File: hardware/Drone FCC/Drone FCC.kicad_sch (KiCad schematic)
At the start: 3 parts, among them J21 Micro_SD_Card_Det_Hirose_DM3AT, J23 47589-0001, U3 STM32F746ZGTx

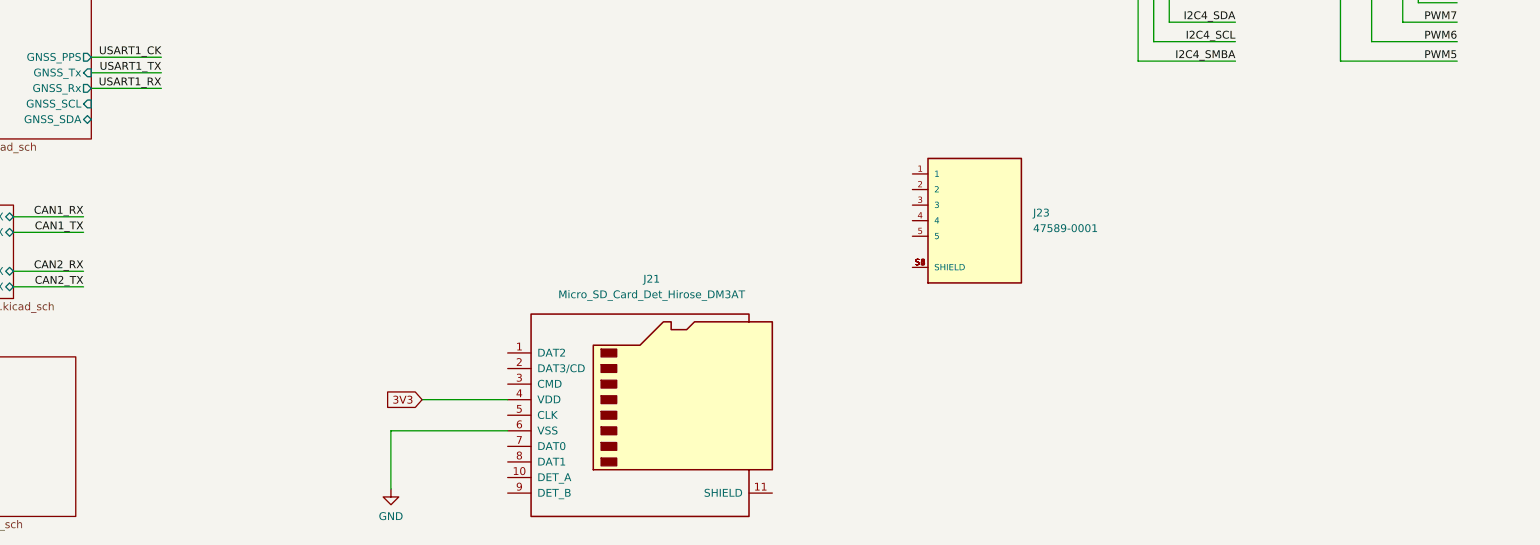
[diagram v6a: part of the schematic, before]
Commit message: DSM: deleted dupont conn, PPM: deleted DF-13 conn
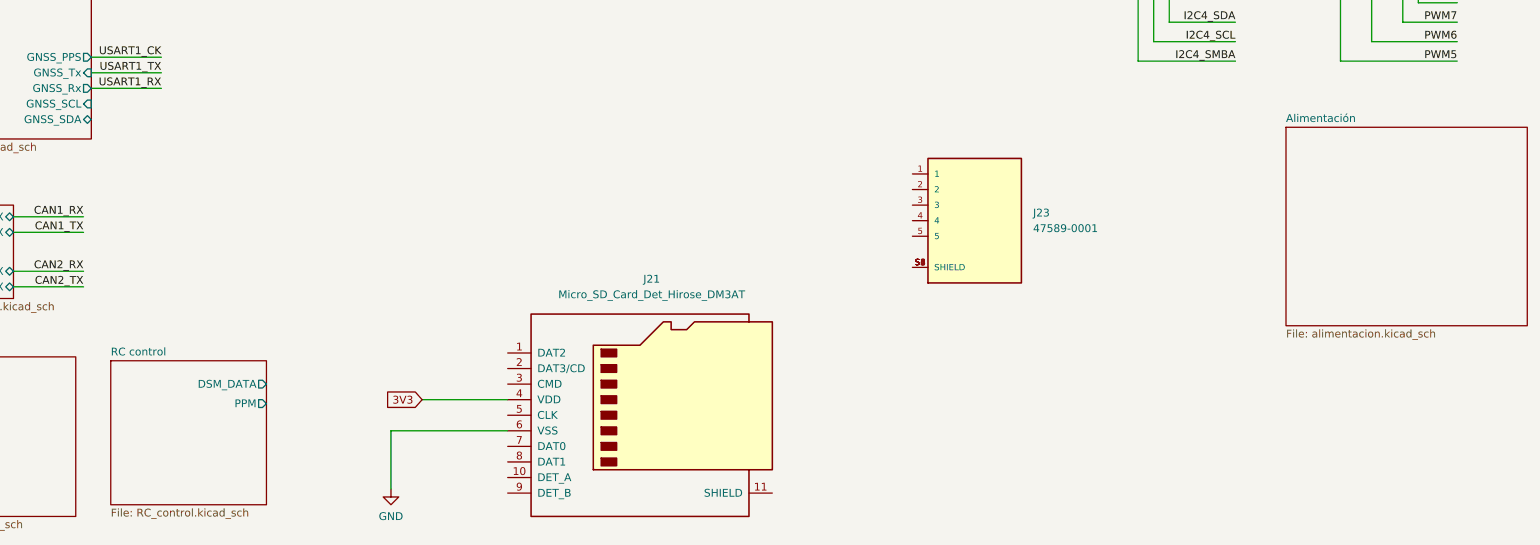
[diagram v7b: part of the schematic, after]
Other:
- added sheet Alimentación (alimentacion.kicad_sch)
- added sheet RC control (RC_control.kicad_sch)
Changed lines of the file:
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@@
+    )
+  )
+  (sheet (at 47.625 166.37) (size 25.4 23.495) (fields_autoplaced)
+    (stroke (width 0.1524) (type solid) (color 0 0 0 0))
+    (fill (color 0 0 0 0.0000))
+    (property "Sheet name" "RC control" (id 0) (at 47.625 165.6584 0)
+      (effects (font (size 1.27 1.27)) (justify left bottom))
+    )
+    (property "Sheet file" "RC_control.kicad_sch" (id 1) (at 47.625 190.4496 0)
+      (effects (font (size 1.27 1.27)) (justify left top))
+    )
+    (pin "DSM_DATA" output (at 73.025 170.18 0)
+      (effects (font (size 1.27 1.27)) (justify right))
+    )
+    (pin "PPM" output (at 73.025 173.355 0)
+      (effects (font (size 1.27 1.27)) (justify right))
+    )
+  )
+  (sheet (at 239.395 128.27) (size 39.37 32.385) (fields_autoplaced)
+    (stroke (width 0.1524) (type solid) (color 0 0 0 0))
+    (fill (color 0 0 0 0.0000))
+    (property "Sheet name" "Alimentación" (id 0) (at 239.395 127.5584 0)
+      (effects (font (size 1.27 1.27)) (justify left bottom))
+    )
+    (property "Sheet file" "alimentacion.kicad_sch" (id 1) (at 239.395 161.2396 0)
+      (effects (font (size 1.27 1.27)) (justify left top))
     )
   )
@@
     (path "/79e0599a-7098-4a96-b5a2-c7f60ed6c34f" (page "5"))
     (path "/f05f239e-e978-4f7d-94d0-b7e31d2fe727" (page "6"))
+    (path "/2e02b919-519b-4cae-a6fb-682f19bf0ab7" (page "6"))
     (path "/2dea4649-a03b-4105-a448-fdfd58cb624b" (page "7"))
+    (path "/72959738-982c-4565-97f6-d336a978e9e3" (page "7"))
   )
   (symbol_instances
@@
       (reference "#PWR0118") (unit 1) (value "GND") (footprint "")
     )
+    (path "/2e02b919-519b-4cae-a6fb-682f19bf0ab7/c452f343-aaf8-46b0-a1d5-405c320adc99"
+      (reference "#PWR0119") (unit 1) (value "GND") (footprint "")
+    )
+    (path "/2e02b919-519b-4cae-a6fb-682f19bf0ab7/ae2e1bfb-335f-4f2d-b7a3-0f7072a0e82b"
+      (reference "#PWR0120") (unit 1) (value "GND") (footprint "")
+    )
+    (path "/72959738-982c-4565-97f6-d336a978e9e3/f8c35dfd-6b96-4fe1-8aab-ccbcdb653023"
+      (reference "#PWR0121") (unit 1) (value "GND") (footprint "")
+    )
     (path "/2dea4649-a03b-4105-a448-fdfd58cb624b/7430465c-9d48-4f87-807f-b7d872f0d403"
       (reference "C1") (unit 1) (value "100n") (footprint "")
@@
     )
     (path "/2dea4649-a03b-4105-a448-fdfd58cb624b/dd0a04d5-6acc-473f-9992-aa28c07b7080"
-      (reference "J1") (unit 1) (value "Conn_02x03_Counter_Clockwise") (footprint "TSW-103-08-G-D-RA:SAMTEC_TSW-103-08-G-D-RA")
+      (reference "J1") (unit 1) (value "Conn_02x03_Counter_Clockwise") (footprint "Connector_PinHeader_2.54mm:PinHeader_2x03_P2.54mm_Horizontal")
     )
     (path "/2dea4649-a03b-4105-a448-fdfd58cb624b/b079b46a-f7fc-473d-a5cf-a695656f1e39"
-      (reference "J2") (unit 1) (value "Conector GPS Auxiliar") (footprint "TSW-103-08-G-D-RA:SAMTEC_TSW-103-08-G-D-RA")
+      (reference "J2") (unit 1) (value "Conector GPS Auxiliar") (footprint "Connector_PinHeader_2.54mm:PinHeader_2x03_P2.54mm_Horizontal")
     )
     (path "/dd9839f2-48a6-46c9-b84f-4c2c3431def5/2c0e7e5c-a396-43ba-a674-e23b0aa3ed8c"
@@
     )
     (path "/dd9839f2-48a6-46c9-b84f-4c2c3431def5/ae1b85cd-d98b-45cf-8891-7b0a605aa920"
-      (reference "J9") (unit 1) (value "Conn_01x03") (footprint "TSW-101-08-G-T-RA:SAMTEC_TSW-101-08-G-T-RA")
+      (reference "J9") (unit 1) (value "Conn_01x03") (footprint "")
     )
     (path "/dd9839f2-48a6-46c9-b84f-4c2c3431def5/a29b1f99-be3b-43d7-88a3-e3ba849894c0"
-      (reference "J10") (unit 1) (value "Conn_01x03") (footprint "TSW-101-08-G-T-RA:SAMTEC_TSW-101-08-G-T-RA")
+      (reference "J10") (unit 1) (value "Conn_01x03") (footprint "")
     )
     (path "/dd9839f2-48a6-46c9-b84f-4c2c3431def5/727e9556-d176-4009-a480-129f163887d1"
-      (reference "J11") (unit 1) (value "Conn_01x03") (footprint "TSW-101-08-G-T-RA:SAMTEC_TSW-101-08-G-T-RA")
+      (reference "J11") (unit 1) (value "Conn_01x03") (footprint "")
     )
     (path "/dd9839f2-48a6-46c9-b84f-4c2c3431def5/e22c99e5-135c-4620-bec6-37c0d91f8aa9"
-      (reference "J12") (unit 1) (value "Conn_01x03") (footprint "TSW-101-08-G-T-RA:SAMTEC_TSW-101-08-G-T-RA")
+      (reference "J12") (unit 1) (value "Conn_01x03") (footprint "")
     )
     (path "/dd9839f2-48a6-46c9-b84f-4c2c3431def5/04df7ea9-ac73-46fd-a164-7c36b6bafc73"
-      (reference "J13") (unit 1) (value "Conn_01x03") (footprint "TSW-101-08-G-T-RA:SAMTEC_TSW-101-08-G-T-RA")
+      (reference "J13") (unit 1) (value "Conn_01x03") (footprint "")
     )
     (path "/dd9839f2-48a6-46c9-b84f-4c2c3431def5/5e787877-d77a-4cee-a93e-1409f44e5225"
-      (reference "J14") (unit 1) (value "Conn_01x03") (footprint "TSW-101-08-G-T-RA:SAMTEC_TSW-101-08-G-T-RA")
+      (reference "J14") (unit 1) (value "Conn_01x03") (footprint "")
     )
     (path "/dd9839f2-48a6-46c9-b84f-4c2c3431def5/003ebe8e-9b64-47ba-9423-d7883e602594"
-      (reference "J15") (unit 1) (value "Conn_01x03") (footprint "TSW-101-08-G-T-RA:SAMTEC_TSW-101-08-G-T-RA")
+      (reference "J15") (unit 1) (value "Conn_01x03") (footprint "")
     )
     (path "/dd9839f2-48a6-46c9-b84f-4c2c3431def5/cb2e432f-bef2-430b-b36c-2c1c24ae2dce"
-      (reference "J16") (unit 1) (value "Conn_01x03") (footprint "TSW-101-08-G-T-RA:SAMTEC_TSW-101-08-G-T-RA")
+      (reference "J16") (unit 1) (value "Conn_01x03") (footprint "")
     )
     (path "/f05f239e-e978-4f7d-94d0-b7e31d2fe727/74b8afda-d0d1-4963-be3e-4a097f544a6e"
-      (reference "J17") (unit 1) (value "Conn_01x04") (footprint "Connector_Hirose:Hirose_DF13C_CL535-0404-8-51_1x04-1MP_P1.25mm_Vertical")
+      (reference "J17") (unit 1) (value "Conn_01x04") (footprint "DF13-4P-1.25H:HRS_DF13-4P-1.25H(75)")
     )
     (path "/f05f239e-e978-4f7d-94d0-b7e31d2fe727/b1ac319c-1524-4124-ba4c-d2671796ddab"
-      (reference "J18") (unit 1) (value "Conn_01x04") (footprint "Connector_Hirose:Hirose_DF13C_CL535-0404-8-51_1x04-1MP_P1.25mm_Vertical")
+      (reference "J18") (unit 1) (value "Conn_01x04") (footprint "DF13-4P-1.25H:HRS_DF13-4P-1.25H(75)")
     )
     (path "/2dea4649-a03b-4105-a448-fdfd58cb624b/b2d2d786-d830-41a8-86bc-a5ceb742f967"
@@
       (reference "J23") (unit 1) (value "47589-0001") (footprint "47589-0001:MOLEX_47589-0001")
     )
+    (path "/2e02b919-519b-4cae-a6fb-682f19bf0ab7/6299bbba-da38-4b1d-aee3-1b5562e402d2"
+      (reference "J24") (unit 1) (value "DSM Spektrum JST") (footprint "B3B-ZR-SM4-TF(LF)(SN):JST-B3B-ZR-SM4-TFLFSN-0-0-MFG")
+    )
+    (path "/2e02b919-519b-4cae-a6fb-682f19bf0ab7/a62587f8-37d8-4b1d-96f5-2656816cd2dc"
+      (reference "J27") (unit 1) (value "PPM Dupont") (footprint "Connector_PinHeader_2.54mm:PinHeader_1x03_P2.54mm_Horizontal")
+    )
+    (path "/72959738-982c-4565-97f6-d336a978e9e3/35d5ea26-c352-4d8a-b32b-9fae6f111b8f"
+      (reference "J28") (unit 1) (value "Conn_01x06") (footprint "Connector_Hirose:Hirose_DF13C_CL535-0406-3-51_1x06-1MP_P1.25mm_Vertical")
+    )
     (path "/2dea4649-a03b-4105-a448-fdfd58cb624b/c6fcfd96-082b-49eb-8c0f-2db889d1df4b"
